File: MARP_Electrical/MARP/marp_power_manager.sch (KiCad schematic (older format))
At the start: 0 parts

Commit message: decided on buck converter and thermocouple ic
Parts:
- added J?: Lane1_CONN, symbol MARP:2x2_Connector
- added R? (x2): R_Small, symbol Device:R_Small
- added U?: LM2576HVS-ADJ(LANE1), Package_TO_SOT_SMD:TO-263-5_TabPin3, symbol Regulator_Switching:LM2576HVS-ADJ
- added U?: MAX31855KASA_, digikey-footprints:SOIC-8_W3.9mm, symbol dk_Interface-Sensor-and-Detector-Interfaces:MAX31855KASA_
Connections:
- new net GND: U?.1 (GND), U?.3 (GND)
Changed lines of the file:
@@
 $Descr A4 11693 8268
 encoding utf-8
-Sheet 1 2
+Sheet 2 2
 Title ""
 Date ""
@@
 Comment4 ""
 $EndDescr
+$Comp
+L Regulator_Switching:LM2576HVS-ADJ U?
+U 1 1 5BC081F3
+P 1500 1800
+F 0 "U?" H 1500 2167 50  0000 C CNN
+F 1 "LM2576HVS-ADJ(LANE1)" H 1500 2076 50  0000 C CNN
+F 2 "Package_TO_SOT_SMD:TO-263-5_TabPin3" H 1500 1550 50  0001 L CIN
+F 3 "http://www.ti.com/lit/ds/symlink/lm2576.pdf" H 1500 1800 50  0001 C CNN
+	1    1500 1800
+	1    0    0    -1
+$EndComp
+$Comp
+L Device:R_Small R?
+U 1 1 5BC0831F
+P 2250 1550
+F 0 "R?" H 2309 1596 50  0000 L CNN
+F 1 "R_Small" H 2309 1505 50  0000 L CNN
+F 2 "" H 2250 1550 50  0001 C CNN
+F 3 "~" H 2250 1550 50  0001 C CNN
+	1    2250 1550
+	1    0    0    -1
+$EndComp
+$Comp
+L Device:R_Small R?
+U 1 1 5BC083A3
+P 2700 1550
+F 0 "R?" H 2759 1596 50  0000 L CNN
+F 1 "R_Small" H 2759 1505 50  0000 L CNN
+F 2 "" H 2700 1550 50  0001 C CNN
+F 3 "~" H 2700 1550 50  0001 C CNN
+	1    2700 1550
+	1    0    0    -1
+$EndComp
+$Comp
+L dk_Interface-Sensor-and-Detector-Interfaces:MAX31855KASA_ U?
+U 1 1 5BC087C9
+P 1250 3100
+F 0 "U?" H 1691 2853 60  0000 L CNN
+F 1 "MAX31855KASA_" H 1691 2747 60  0000 L CNN
+F 2 "digikey-footprints:SOIC-8_W3.9mm" H 1450 3300 60  0001 L CNN
+F 3 "https://datasheets.maximintegrated.com/en/ds/MAX31855.pdf" H 1450 3400 60  0001 L CNN
+F 4 "MAX31855KASA+-ND" H 1450 3500 60  0001 L CNN "Digi-Key_PN"
+F 5 "MAX31855KASA+" H 1450 3600 60  0001 L CNN "MPN"
+F 6 "Integrated Circuits (ICs)" H 1450 3700 60  0001 L CNN "Category"
+F 7 "Interface - Sensor and Detector Interfaces" H 1450 3800 60  0001 L CNN "Family"
+F 8 "https://datasheets.maximintegrated.com/en/ds/MAX31855.pdf" H 1450 3900 60  0001 L CNN "DK_Datasheet_Link"
+F 9 "/product-detail/en/maxim-integrated/MAX31855KASA-/MAX31855KASA--ND/2591564" H 1450 4000 60  0001 L CNN "DK_Detail_Page"
+F 10 "IC CONV THERMOCOUPLE-DGTL SOIC" H 1450 4100 60  0001 L CNN "Description"
+F 11 "Maxim Integrated" H 1450 4200 60  0001 L CNN "Manufacturer"
+F 12 "Active" H 1450 4300 60  0001 L CNN "Status"
+	1    1250 3100
+	1    0    0    -1
+$EndComp
+Wire Wire Line
+	1450 3800 1450 4000
+$Comp
+L power:GND #PWR?
+U 1 1 5BC0949D
+P 1450 4000
+F 0 "#PWR?" H 1450 3750 50  0001 C CNN
+F 1 "GND" H 1455 3827 50  0000 C CNN
+F 2 "" H 1450 4000 50  0001 C CNN
+F 3 "" H 1450 4000 50  0001 C CNN
+	1    1450 4000
+	1    0    0    -1
+$EndComp
+$Comp
+L MARP:2x2_Connector J?
+U 1 1 5BC2CD48
+P 1450 1050
+F 0 "J?" H 1475 1465 50  0000 C CNN
+F 1 "Lane1_CONN" H 1475 1374 50  0000 C CNN
+F 2 "" H 1550 1050 50  0001 C CNN
+F 3 "" H 1550 1050 50  0001 C CNN
+	1    1450 1050
+	1    0    0    -1
+$EndComp
+$Comp
+L power:GND #PWR?
+U 1 1 5BC2D3FD
+P 1500 2250
+F 0 "#PWR?" H 1500 2000 50  0001 C CNN
+F 1 "GND" H 1505 2077 50  0000 C CNN
+F 2 "" H 1500 2250 50  0001 C CNN
+F 3 "" H 1500 2250 50  0001 C CNN
+	1    1500 2250
+	1    0    0    -1
+$EndComp
+Wire Wire Line
+	1500 2100 1500 2250
 $EndSCHEMATC

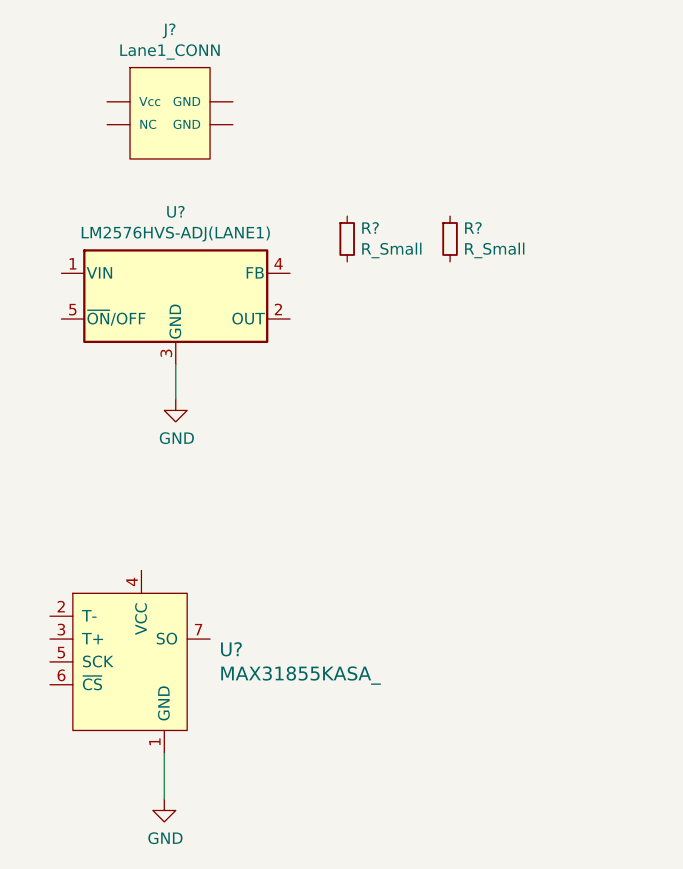
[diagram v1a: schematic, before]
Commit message: thermocouple testing
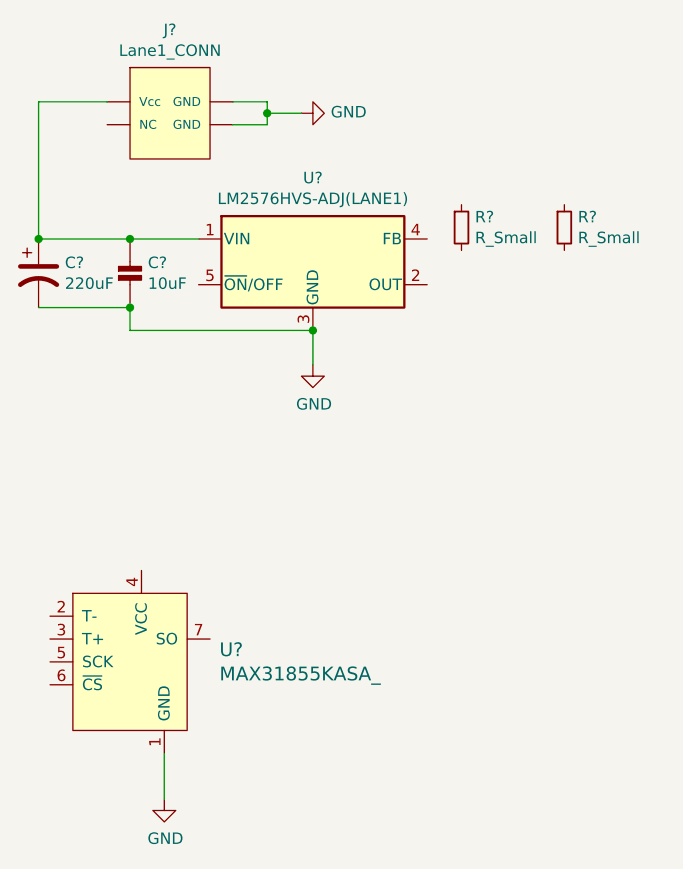
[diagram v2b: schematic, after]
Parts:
- added C?: 220uF, symbol Device:CP1
- added C?: 10uF, symbol MAX31855:CAP_CERAMIC0603
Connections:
- net GND: now also J?.~ (Vcc), C?.2, C?.2 (P$2)
- net at U?.1 (VIN): now also J?.~ (Vcc), C?.1, C?.1 (P$1)
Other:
- moved on the sheet: R?, U?
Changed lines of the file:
@@
 L Regulator_Switching:LM2576HVS-ADJ U?
 U 1 1 5BC081F3
-P 1500 1800
-F 0 "U?" H 1500 2167 50  0000 C CNN
-F 1 "LM2576HVS-ADJ(LANE1)" H 1500 2076 50  0000 C CNN
-F 2 "Package_TO_SOT_SMD:TO-263-5_TabPin3" H 1500 1550 50  0001 L CIN
-F 3 "http://www.ti.com/lit/ds/symlink/lm2576.pdf" H 1500 1800 50  0001 C CNN
-	1    1500 1800
+P 2100 1650
+F 0 "U?" H 2100 2017 50  0000 C CNN
+F 1 "LM2576HVS-ADJ(LANE1)" H 2100 1926 50  0000 C CNN
+F 2 "Package_TO_SOT_SMD:TO-263-5_TabPin3" H 2100 1400 50  0001 L CIN
+F 3 "http://www.ti.com/lit/ds/symlink/lm2576.pdf" H 2100 1650 50  0001 C CNN
+	1    2100 1650
 	1    0    0    -1
 $EndComp
@@
 L Device:R_Small R?
 U 1 1 5BC0831F
-P 2250 1550
-F 0 "R?" H 2309 1596 50  0000 L CNN
-F 1 "R_Small" H 2309 1505 50  0000 L CNN
-F 2 "" H 2250 1550 50  0001 C CNN
-F 3 "~" H 2250 1550 50  0001 C CNN
-	1    2250 1550
+P 2750 1500
+F 0 "R?" H 2809 1546 50  0000 L CNN
+F 1 "R_Small" H 2809 1455 50  0000 L CNN
+F 2 "" H 2750 1500 50  0001 C CNN
+F 3 "~" H 2750 1500 50  0001 C CNN
+	1    2750 1500
 	1    0    0    -1
 $EndComp
@@
 L Device:R_Small R?
 U 1 1 5BC083A3
-P 2700 1550
-F 0 "R?" H 2759 1596 50  0000 L CNN
-F 1 "R_Small" H 2759 1505 50  0000 L CNN
-F 2 "" H 2700 1550 50  0001 C CNN
-F 3 "~" H 2700 1550 50  0001 C CNN
-	1    2700 1550
+P 3200 1500
+F 0 "R?" H 3259 1546 50  0000 L CNN
+F 1 "R_Small" H 3259 1455 50  0000 L CNN
+F 2 "" H 3200 1500 50  0001 C CNN
+F 3 "~" H 3200 1500 50  0001 C CNN
+	1    3200 1500
 	1    0    0    -1
 $EndComp
@@
 L power:GND #PWR?
 U 1 1 5BC2D3FD
-P 1500 2250
-F 0 "#PWR?" H 1500 2000 50  0001 C CNN
-F 1 "GND" H 1505 2077 50  0000 C CNN
-F 2 "" H 1500 2250 50  0001 C CNN
-F 3 "" H 1500 2250 50  0001 C CNN
-	1    1500 2250
+P 2100 2100
+F 0 "#PWR?" H 2100 1850 50  0001 C CNN
+F 1 "GND" H 2105 1927 50  0000 C CNN
+F 2 "" H 2100 2100 50  0001 C CNN
+F 3 "" H 2100 2100 50  0001 C CNN
+	1    2100 2100
 	1    0    0    -1
 $EndComp
 Wire Wire Line
-	1500 2100 1500 2250
+	2100 1950 2100 2100
+$Comp
+L Device:CP1 C?
+U 1 1 5BC33E9C
+P 900 1700
+F 0 "C?" H 1015 1746 50  0000 L CNN
+F 1 "220uF" H 1015 1655 50  0000 L CNN
+F 2 "" H 900 1700 50  0001 C CNN
+F 3 "~" H 900 1700 50  0001 C CNN
+	1    900  1700
+	1    0    0    -1
+$EndComp
+$Comp
+L MAX31855:CAP_CERAMIC0603 C?
+U 1 1 5BC34D59
+P 1300 1750
+F 0 "C?" H 1378 1846 50  0000 L CNN
+F 1 "10uF" H 1378 1755 50  0000 L CNN
+F 2 "" H 1300 1750 50  0001 C CNN
+F 3 "" H 1300 1750 50  0001 C CNN
+	1    1300 1750
+	1    0    0    -1
+$EndComp
+Wire Wire Line
+	1200 950  900  950
+Wire Wire Line
+	900  950  900  1550
+Wire Wire Line
+	1750 950  1900 950
+Wire Wire Line
+	1900 950  1900 1000
+Wire Wire Line
+	1900 1050 1750 1050
+Wire Wire Line
+	1900 1000 2050 1000
+Connection ~ 1900 1000
+Wire Wire Line
+	1900 1000 1900 1050
+$Comp
+L power:GND #PWR?
+U 1 1 5BC34FBE
+P 2050 1000
+F 0 "#PWR?" H 2050 750 50  0001 C CNN
+F 1 "GND" V 2055 872 50  0000 R CNN
+F 2 "" H 2050 1000 50  0001 C CNN
+F 3 "" H 2050 1000 50  0001 C CNN
+	1    2050 1000
+	0    -1   -1   0
+$EndComp
+Wire Wire Line
+	900  1850 1300 1850
+Wire Wire Line
+	1300 1850 1300 1950
+Wire Wire Line
+	1300 1950 2100 1950
+Connection ~ 1300 1850
+Connection ~ 2100 1950
+Wire Wire Line
+	900  1550 1300 1550
+Connection ~ 900  1550
+Wire Wire Line
+	1300 1550 1600 1550
+Connection ~ 1300 1550
 $EndSCHEMATC

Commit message: Added sd card holder, logic level shifter, fets for power source logic; removed old stuff
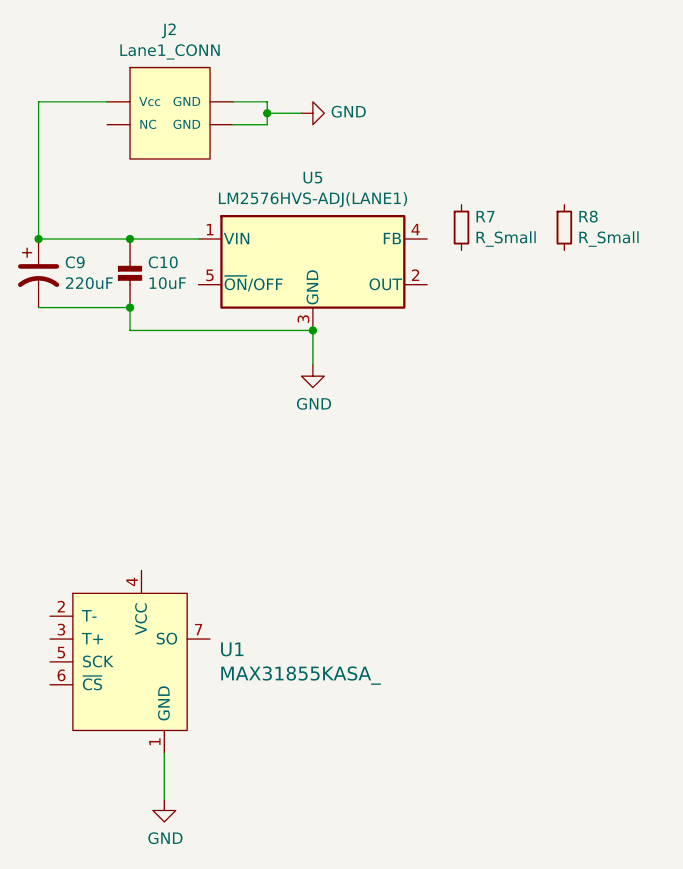
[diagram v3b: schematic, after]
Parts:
- gave numbers to parts that had none: 7
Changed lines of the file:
@@
 $EndDescr
 $Comp
-L Regulator_Switching:LM2576HVS-ADJ U?
+L Regulator_Switching:LM2576HVS-ADJ U5
 U 1 1 5BC081F3
 P 2100 1650
-F 0 "U?" H 2100 2017 50  0000 C CNN
+F 0 "U5" H 2100 2017 50  0000 C CNN
 F 1 "LM2576HVS-ADJ(LANE1)" H 2100 1926 50  0000 C CNN
 F 2 "Package_TO_SOT_SMD:TO-263-5_TabPin3" H 2100 1400 50  0001 L CIN
@@
 $EndComp
 $Comp
-L Device:R_Small R?
+L Device:R_Small R7
 U 1 1 5BC0831F
 P 2750 1500
-F 0 "R?" H 2809 1546 50  0000 L CNN
+F 0 "R7" H 2809 1546 50  0000 L CNN
 F 1 "R_Small" H 2809 1455 50  0000 L CNN
 F 2 "" H 2750 1500 50  0001 C CNN
@@
 $EndComp
 $Comp
-L Device:R_Small R?
+L Device:R_Small R8
 U 1 1 5BC083A3
 P 3200 1500
-F 0 "R?" H 3259 1546 50  0000 L CNN
+F 0 "R8" H 3259 1546 50  0000 L CNN
 F 1 "R_Small" H 3259 1455 50  0000 L CNN
 F 2 "" H 3200 1500 50  0001 C CNN
@@
 $EndComp
 $Comp
-L dk_Interface-Sensor-and-Detector-Interfaces:MAX31855KASA_ U?
+L dk_Interface-Sensor-and-Detector-Interfaces:MAX31855KASA_ U1
 U 1 1 5BC087C9
 P 1250 3100
-F 0 "U?" H 1691 2853 60  0000 L CNN
+F 0 "U1" H 1691 2853 60  0000 L CNN
 F 1 "MAX31855KASA_" H 1691 2747 60  0000 L CNN
 F 2 "digikey-footprints:SOIC-8_W3.9mm" H 1450 3300 60  0001 L CNN
@@
 	1450 3800 1450 4000
 $Comp
-L power:GND #PWR?
+L power:GND #PWR0111
 U 1 1 5BC0949D
 P 1450 4000
-F 0 "#PWR?" H 1450 3750 50  0001 C CNN
+F 0 "#PWR0111" H 1450 3750 50  0001 C CNN
 F 1 "GND" H 1455 3827 50  0000 C CNN
 F 2 "" H 1450 4000 50  0001 C CNN
@@
 $EndComp
 $Comp
-L MARP:2x2_Connector J?
+L MARP:2x2_Connector J2
 U 1 1 5BC2CD48
 P 1450 1050
-F 0 "J?" H 1475 1465 50  0000 C CNN
+F 0 "J2" H 1475 1465 50  0000 C CNN
 F 1 "Lane1_CONN" H 1475 1374 50  0000 C CNN
 F 2 "" H 1550 1050 50  0001 C CNN
@@
 $EndComp
 $Comp
-L power:GND #PWR?
+L power:GND #PWR0112
 U 1 1 5BC2D3FD
 P 2100 2100
-F 0 "#PWR?" H 2100 1850 50  0001 C CNN
+F 0 "#PWR0112" H 2100 1850 50  0001 C CNN
 F 1 "GND" H 2105 1927 50  0000 C CNN
 F 2 "" H 2100 2100 50  0001 C CNN
@@
 	2100 1950 2100 2100
 $Comp
-L Device:CP1 C?
+L Device:CP1 C9
 U 1 1 5BC33E9C
 P 900 1700
-F 0 "C?" H 1015 1746 50  0000 L CNN
+F 0 "C9" H 1015 1746 50  0000 L CNN
 F 1 "220uF" H 1015 1655 50  0000 L CNN
 F 2 "" H 900 1700 50  0001 C CNN
@@
 $EndComp
 $Comp
-L MAX31855:CAP_CERAMIC0603 C?
+L MAX31855:CAP_CERAMIC0603 C10
 U 1 1 5BC34D59
 P 1300 1750
-F 0 "C?" H 1378 1846 50  0000 L CNN
+F 0 "C10" H 1378 1846 50  0000 L CNN
 F 1 "10uF" H 1378 1755 50  0000 L CNN
 F 2 "" H 1300 1750 50  0001 C CNN
@@
 	1900 1000 1900 1050
 $Comp
-L power:GND #PWR?
+L power:GND #PWR0113
 U 1 1 5BC34FBE
 P 2050 1000
-F 0 "#PWR?" H 2050 750 50  0001 C CNN
+F 0 "#PWR0113" H 2050 750 50  0001 C CNN
 F 1 "GND" V 2055 872 50  0000 R CNN
 F 2 "" H 2050 1000 50  0001 C CNN
